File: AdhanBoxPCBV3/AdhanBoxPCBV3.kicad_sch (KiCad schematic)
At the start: 38 parts, among them J1 microSD, J2 SPEAKER 4-8ohm, J3 USB-C 16P, J4 TTP223 3V3/SIG/GND, J5 LED 5V/DATA/GND, J6 SPEAKER 2 (8ohm si x2), J7 5V INPUT (alt), SW1 RESET, SW2 BOOT, U1 ESP32-S3-WROOM-1-N4R2, U2 MAX98357A, U3 RX8025T, U4 AMS1117-3.3

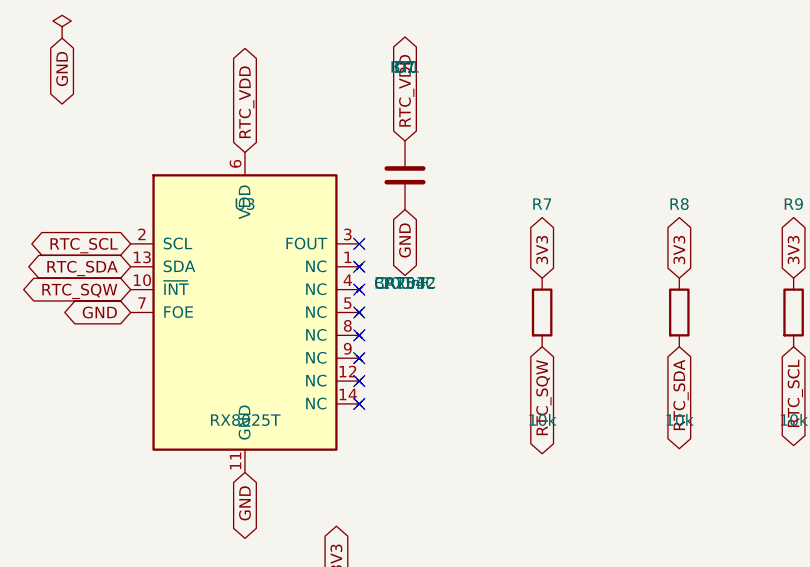
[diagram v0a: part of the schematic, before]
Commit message: PCB V3 : routage complet de la pile de secours RTC en face arriere
- D1 BAT54C (SOT-23) et BT1 support CR1225 (Keystone 3000) places cote soudure
- Ilot RTC_VDD isole du 3V3 (pull-up R7 conserve sur 3V3)
- C7 et D1.p3 relies par la face arriere, alimentation D1.p1 via stub R7
- Route RTC_BATT 100% B.Cu sans via par le bord Est (x=186.9)
- Pontet entre les deux clips du support pile
- DRC : 0 court-circuit, 0 croisement, non-connectes = base (2 zones GND)
- BOM : support CR2032/Keystone 3034 -> CR1225/Keystone 3000 (~7 ans a 0.75uA)

Co-Authored-By: Claude Fable 5 <noreply@anthropic.com>
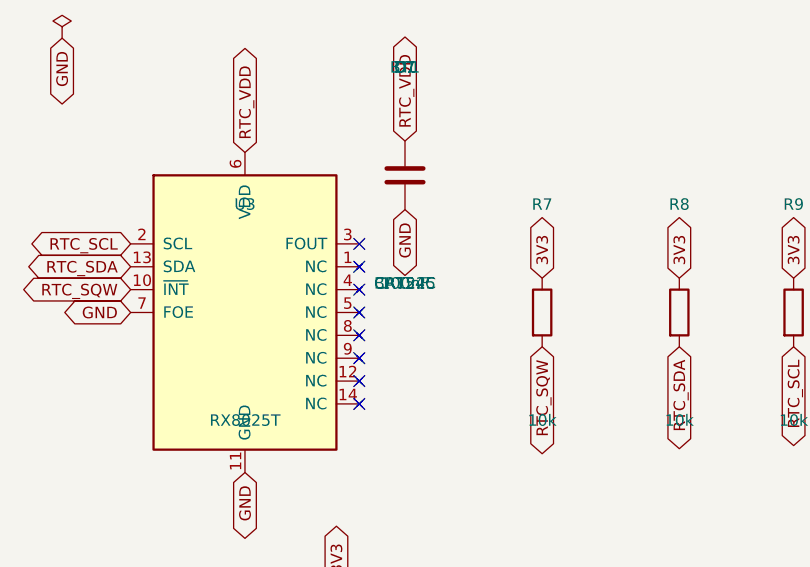
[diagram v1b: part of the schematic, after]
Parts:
- BT1: value CR2032 -> CR1225; footprint Battery:BatteryHolder_Keystone_3034_1x20mm -> Battery:BatteryHolder_Keystone_3000_1x12mm
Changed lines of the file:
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@@
 			(effects (font (size 1.27 1.27)))
 		)
-		(property "Value" "CR2032"
+		(property "Value" "CR1225"
 			(at 78.74 57.72 0)
 			(effects (font (size 1.27 1.27)))
 		)
-		(property "Footprint" "Battery:BatteryHolder_Keystone_3034_1x20mm"
+		(property "Footprint" "Battery:BatteryHolder_Keystone_3000_1x12mm"
 			(at 78.74 45.72 0)
 			(effects (font (size 1.27 1.27)) (hide yes))
